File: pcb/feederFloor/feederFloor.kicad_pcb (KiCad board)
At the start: 2 copper layers, 13.5 x 42.9 mm, 10 parts, among them J1 IDC, J2 Conn_01x10_Female, U1 DS2431

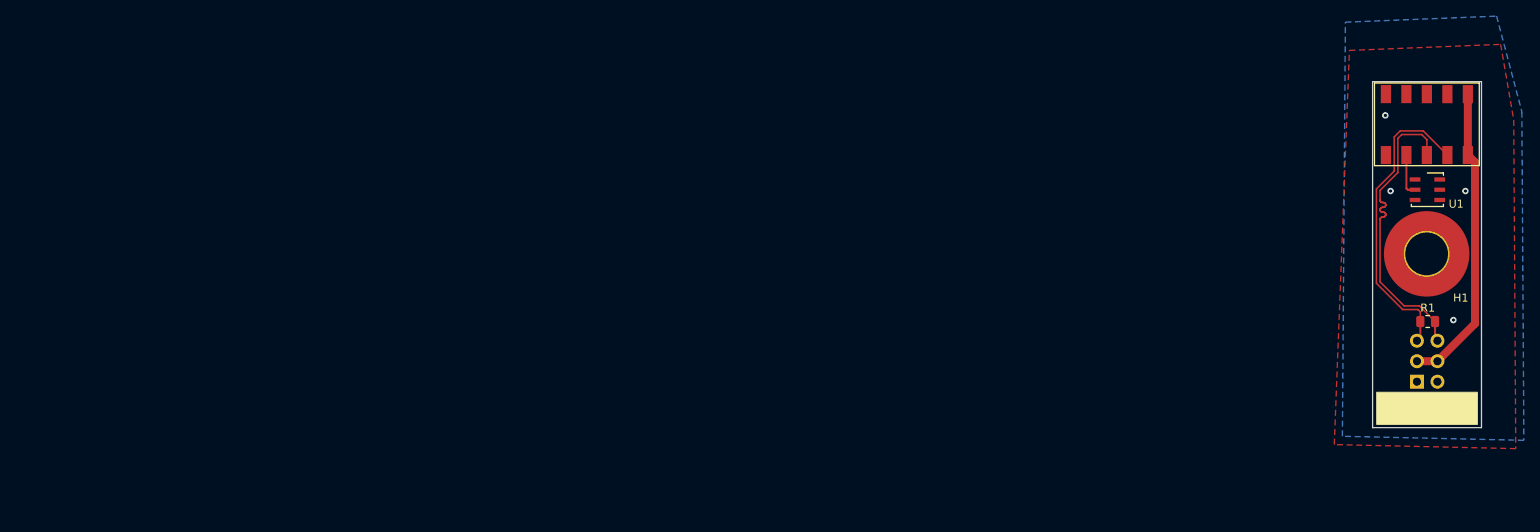
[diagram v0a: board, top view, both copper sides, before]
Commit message: represents rev07 feeder controller, rev03 indexing wheel, rev03 feeder floor. also checks in lots of cad work for feeder design and feeder floor design
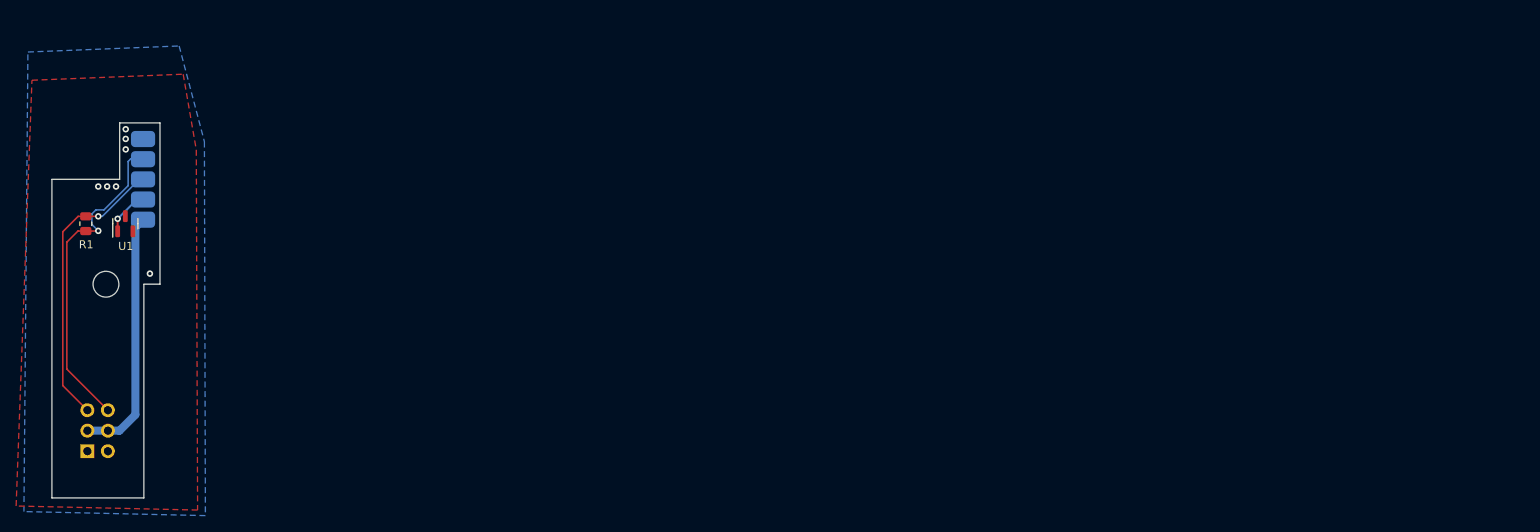
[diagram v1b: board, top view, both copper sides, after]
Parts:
- removed G***: LOGO, index:logo
- removed svg2mod (x4): G***, label
- H1: footprint MountingHole:MountingHole_5.3mm_M5_Pad_TopOnly -> MountingHole:MountingHole_3.2mm_M3
- J2: value Conn_01x10_Female -> Conn_01x05_Female; footprint index:70AA-5 -> feeder:AVX-915-005-541-Contact-Surface; moved to B.Cu
- U1: value DS2431 -> DS28E05; footprint Package_SO_J-Lead:TSOC-6_3.76x3.94mm_P1.27mm -> Package_TO_SOT_SMD:SOT-23
- moved R1 166.8 mm to (25.5, 37.6), turned to 90 degrees
- moved J1 165.1 mm to (25.7, 65.8)
- moved H1 163.8 mm to (28.0, 45.1)
- moved U1 161.5 mm to (30.4, 37.6), turned to 90 degrees
- moved J2 154.1 mm to (32.6, 27.1), turned to -90 degrees
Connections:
- J2 pad 2: 1WIRE -> RS-485-
- J2 pad 3: RS-485- -> RS-485+
- J2 pad 4: RS-485+ -> 1WIRE
- U1 pad 1: GND -> 1WIRE
- U1 pad 2: 1WIRE -> unconnected-(U1-Pad2)
- U1 pad 3: Net-(U1-Pad3) -> GND
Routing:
- net VIN: track 37.9 -> 31.3 mm
- net RS-485-: track 37.8 -> 40.8 mm, vias 0 -> 1
- net RS-485+: track 37.9 -> 36.0 mm, vias 0 -> 1
- net 1WIRE: track 5.28 -> 5.69 mm, vias 0 -> 1
- net GND: vias 4 -> 7
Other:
- board size 13.5 x 42.9 mm -> 13.4 x 46.5 mm
- board text added: "Feeder Floor REV03"
- board text removed: "<<hash>>"

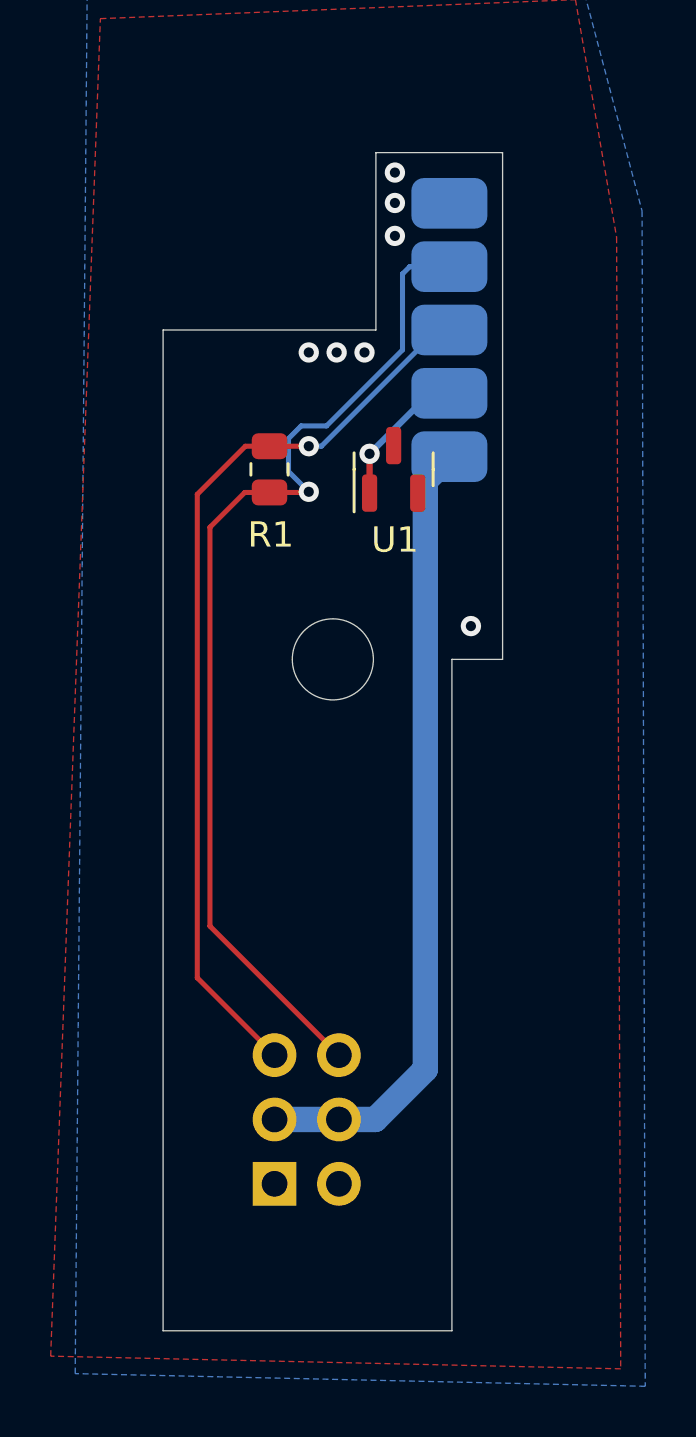
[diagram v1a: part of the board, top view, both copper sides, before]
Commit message: moved feeder motherboard geometry so spring fingers come straight down onto pads
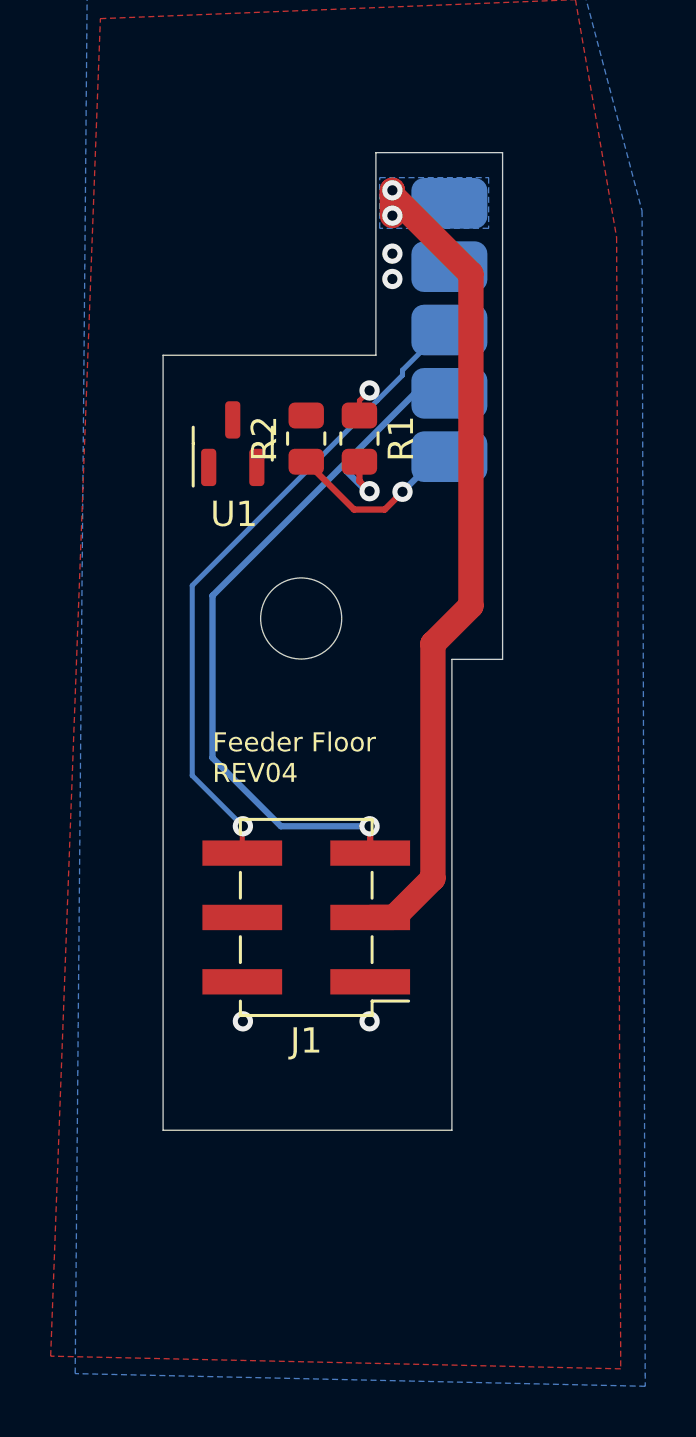
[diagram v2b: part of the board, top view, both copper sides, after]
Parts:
- added R2: 1M, Resistor_SMD:R_0805_2012Metric, F.Cu at (26.9, 36.4)
- J1: footprint Connector_IDC:IDC-Header_2x03_P2.54mm_Vertical -> Connector_PinHeader_2.54mm:PinHeader_2x03_P2.54mm_Vertical_SMD; moved to F.Cu
- moved J1 10.6 mm to (26.9, 55.3), turned to 180 degrees
- moved U1 6.43 mm to (24.0, 36.6)
- moved R1 3.75 mm to (29.0, 36.4), turned to -90 degrees
- moved H1 2.04 mm to (26.7, 43.5)
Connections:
- J2 pad 1: GND -> VIN
- J2 pad 2: RS-485- -> GND
- J2 pad 3: RS-485+ -> RS-485-
- J2 pad 4: 1WIRE -> RS-485+
- J2 pad 5: VIN -> 1WIRE
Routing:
- net RS-485-: track 40.8 -> 27.2 mm, vias 1 -> 2
- net RS-485+: track 36.0 -> 30.3 mm, vias 1 -> 2
- net VIN: track 31.3 -> 36.6 mm, vias 0 -> 2
- net 1WIRE: track 5.69 -> 7.64 mm
- net GND: vias 7 -> 4
- added copper zone on B.Cu, net VIN
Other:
- board size 13.4 x 46.5 mm -> 13.4 x 38.6 mm
- board text added: "Feeder Floor REV04"
- board text removed: "Feeder Floor REV03"

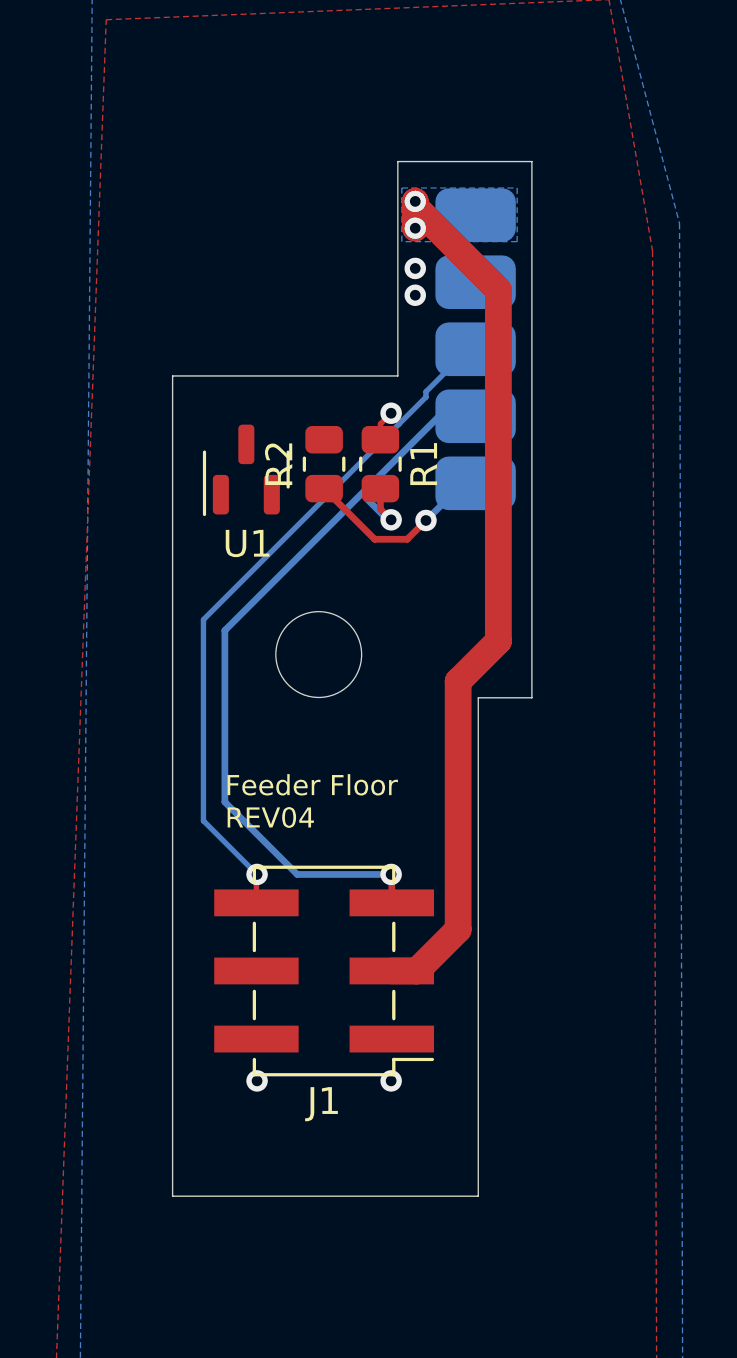
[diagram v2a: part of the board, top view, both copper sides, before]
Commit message: represents rev08 of feeder controller, rev04 of feeder floor. cad still needs some tweaks.
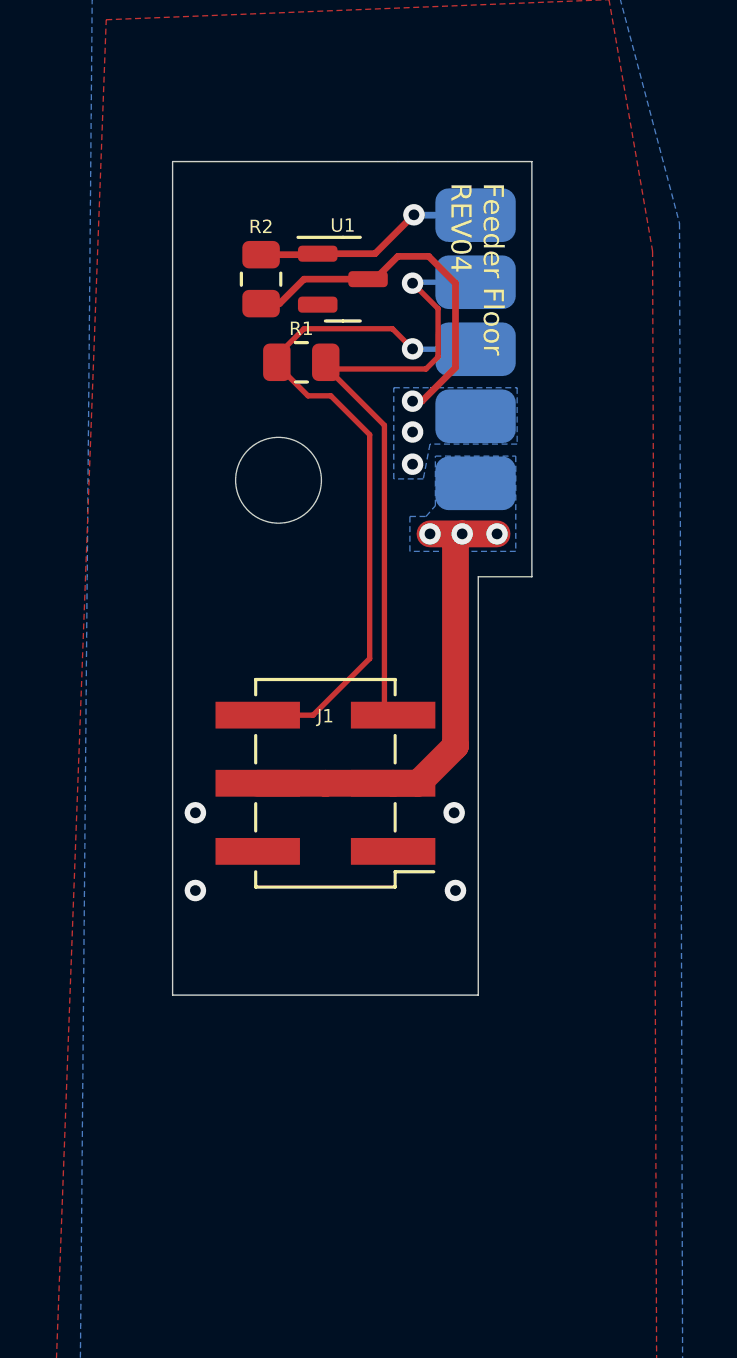
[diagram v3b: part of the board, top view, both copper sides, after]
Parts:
- added G***: LOGO, index:logo, B.Cu at (26.9, 50.5)
- moved U1 7.96 mm to (27.6, 29.5), turned to 0 degrees
- moved R2 7.29 mm to (24.6, 29.5), turned to -90 degrees
- moved J1 7.00 mm to (26.9, 48.3)
- moved H1 6.67 mm to (25.2, 37.0)
- moved R1 4.81 mm to (26.1, 32.6), turned to 0 degrees
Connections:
- J2 pad 1: VIN -> 1WIRE
- J2 pad 2: GND -> RS-485+
- J2 pad 4: RS-485+ -> GND
- J2 pad 5: 1WIRE -> VIN
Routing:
- net VIN: track 36.6 -> 18.5 mm, vias 2 -> 3
- net GND: track 0.00 -> 13.7 mm, vias 4 -> 7
- net RS-485+: track 30.3 -> 24.2 mm, vias 2 -> 1
- net 1WIRE: track 7.64 -> 8.62 mm
- net RS-485-: track 27.2 -> 26.4 mm, vias 2 -> 1
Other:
- board size 13.4 x 38.6 mm -> 13.4 x 31.1 mm

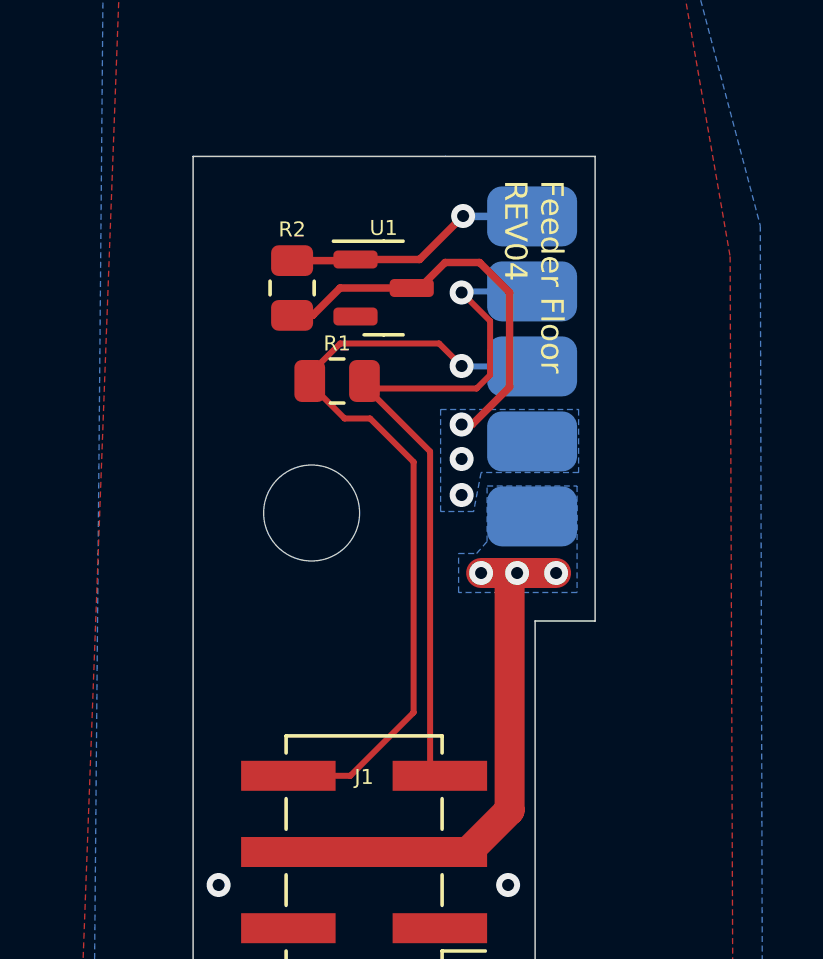
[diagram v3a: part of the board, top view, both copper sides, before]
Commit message: this commit represents rev09 of the controller, rev04 of the indexing wheel, and rev05 of the feeder floor
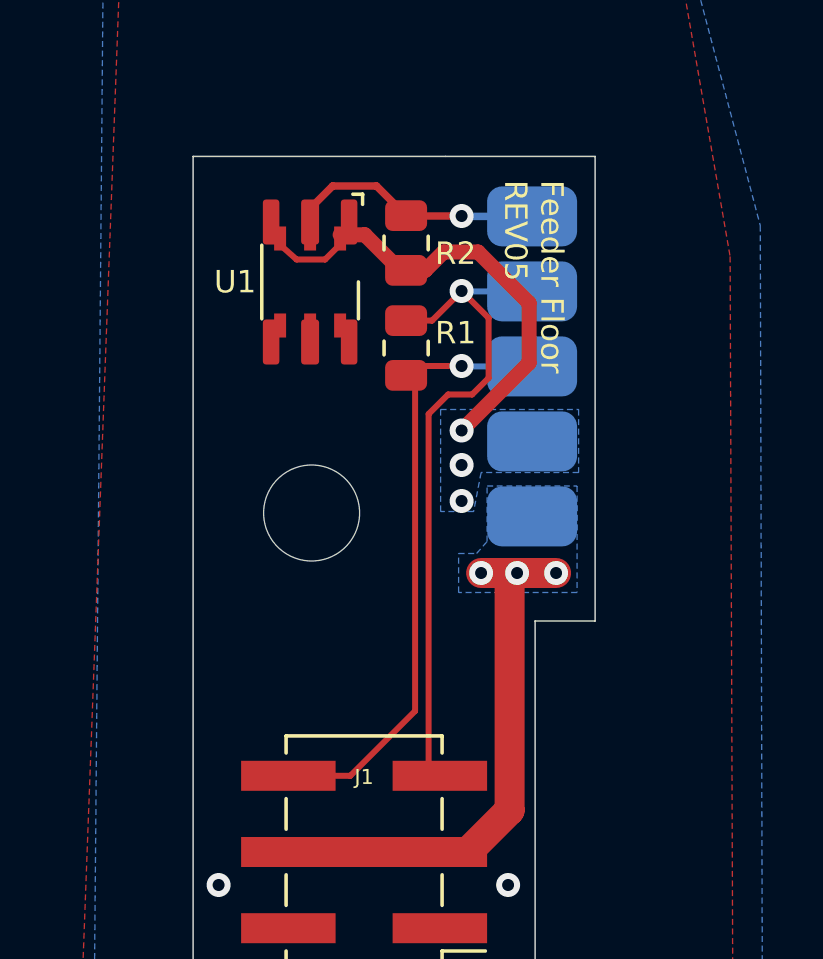
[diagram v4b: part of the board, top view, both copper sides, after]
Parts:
- U1: value DS28E05 -> DS28E07; footprint Package_TO_SOT_SMD:SOT-23 -> feeder:DS28E07_MULTI
- moved R2 4.09 mm to (28.4, 28.0)
- moved R1 2.55 mm to (28.4, 31.5), turned to 90 degrees
- moved U1 2.46 mm to (25.1, 29.3), turned to -90 degrees
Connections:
- U1 pad 1: 1WIRE -> GND
- U1 pad 2: unconnected-(U1-Pad2) -> 1WIRE
- U1 pad 3: GND -> (no net)
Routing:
- net RS-485-: track 26.4 -> 20.8 mm
- net RS-485+: track 24.2 -> 22.6 mm
- net GND: track 13.7 -> 12.9 mm
- net 1WIRE: track 8.62 -> 9.13 mm
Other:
- board text added: "Feeder Floor REV05"
- board text removed: "Feeder Floor REV04"
